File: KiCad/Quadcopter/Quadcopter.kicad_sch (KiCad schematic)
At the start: 20 parts, among them J1 Conn_01x06, J2 Conn_01x03, J3 Conn_01x03, J4 Conn_01x04, J5 Conn_02x04_Odd_Even, J6 Conn_01x04, J7 Screw_Terminal_01x02, U1 BMP388, U2 ICM-20948_CJMCU, U3 Teensy4.1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

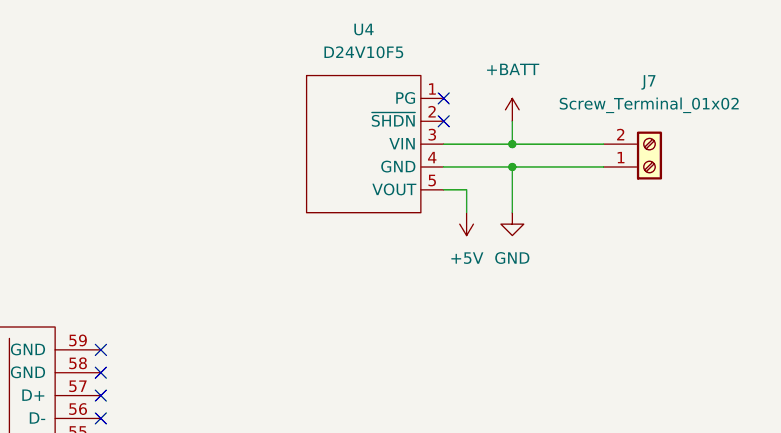
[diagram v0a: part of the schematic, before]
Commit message: - use screwless terminal block with side entry for power - use more generic pressure sensor name and more generic 5V DC-DC converter - add PCB name and date
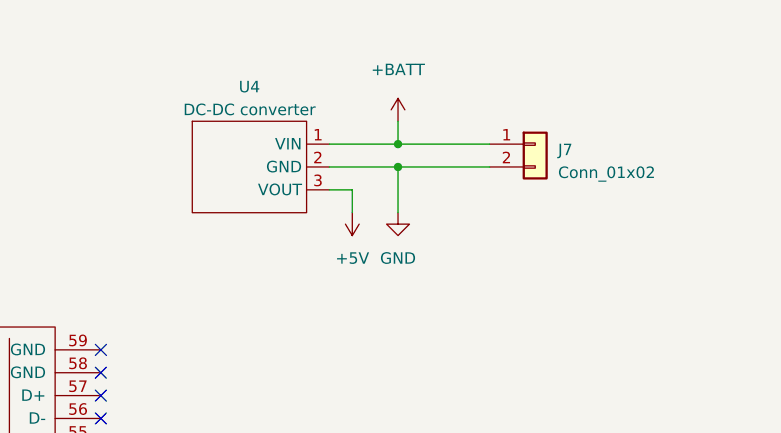
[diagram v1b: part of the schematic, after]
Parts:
- removed J7: Screw_Terminal_01x02, TerminalBlock_Phoenix:TerminalBlock_Phoenix_MPT-0,5-2-2.54_1x02_P2.54mm_Horizontal, symbol Connector:Screw_Terminal_01x02
- removed U4: D24V10F5, Lukas:D24V10F5, symbol Lukas:D24V10F5
- added J7: Conn_01x02, Quadcopter:691402910002B, symbol Connector_Generic:Conn_01x02
- added U4: DC-DC converter, Lukas:DC-DC converter, symbol Lukas:DC-DC converter
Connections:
- net +5V: now also U4.3 (VOUT)
- net +BATT: now also J7.1 (Pin_1), U4.1 (VIN)
- net GND: now also J7.2 (Pin_2), U4.2 (GND)
- no-connect marks 42 -> 40
